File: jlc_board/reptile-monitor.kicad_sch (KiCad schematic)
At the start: 49 parts, among them J1 USB_C_Receptacle_USB2.0, J2 AC_IN, J3 Conn_01x08, J7 LOAD0, J8 LOAD1, K1 1462041-7, K2 1462041-7, SW1 RESET, SW2 BOOT, U1 ESP32-S2-WROVER, U2 TPS2112PW, U3 AP2112K-3.3, U4 MDC3105LT1G, U5 MDC3105LT1G, Y1 32.768KHz 12.5p

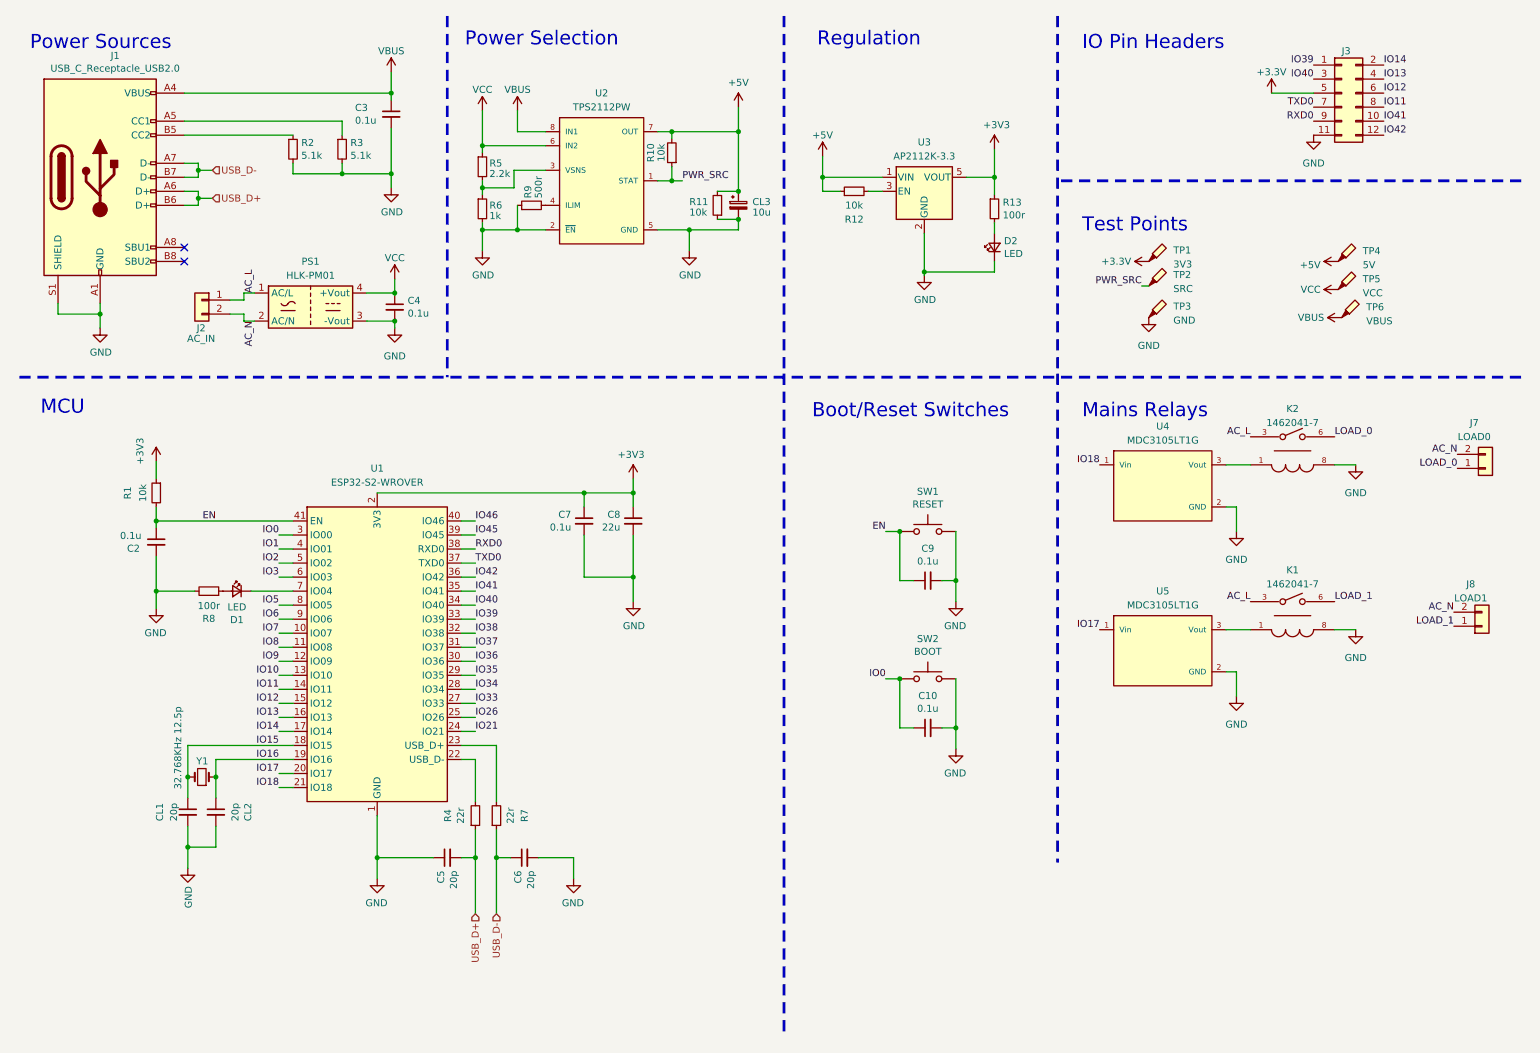
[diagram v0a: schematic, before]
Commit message: Rev2 - Change to Panasonic relays as they're actually attainable and cheaper.
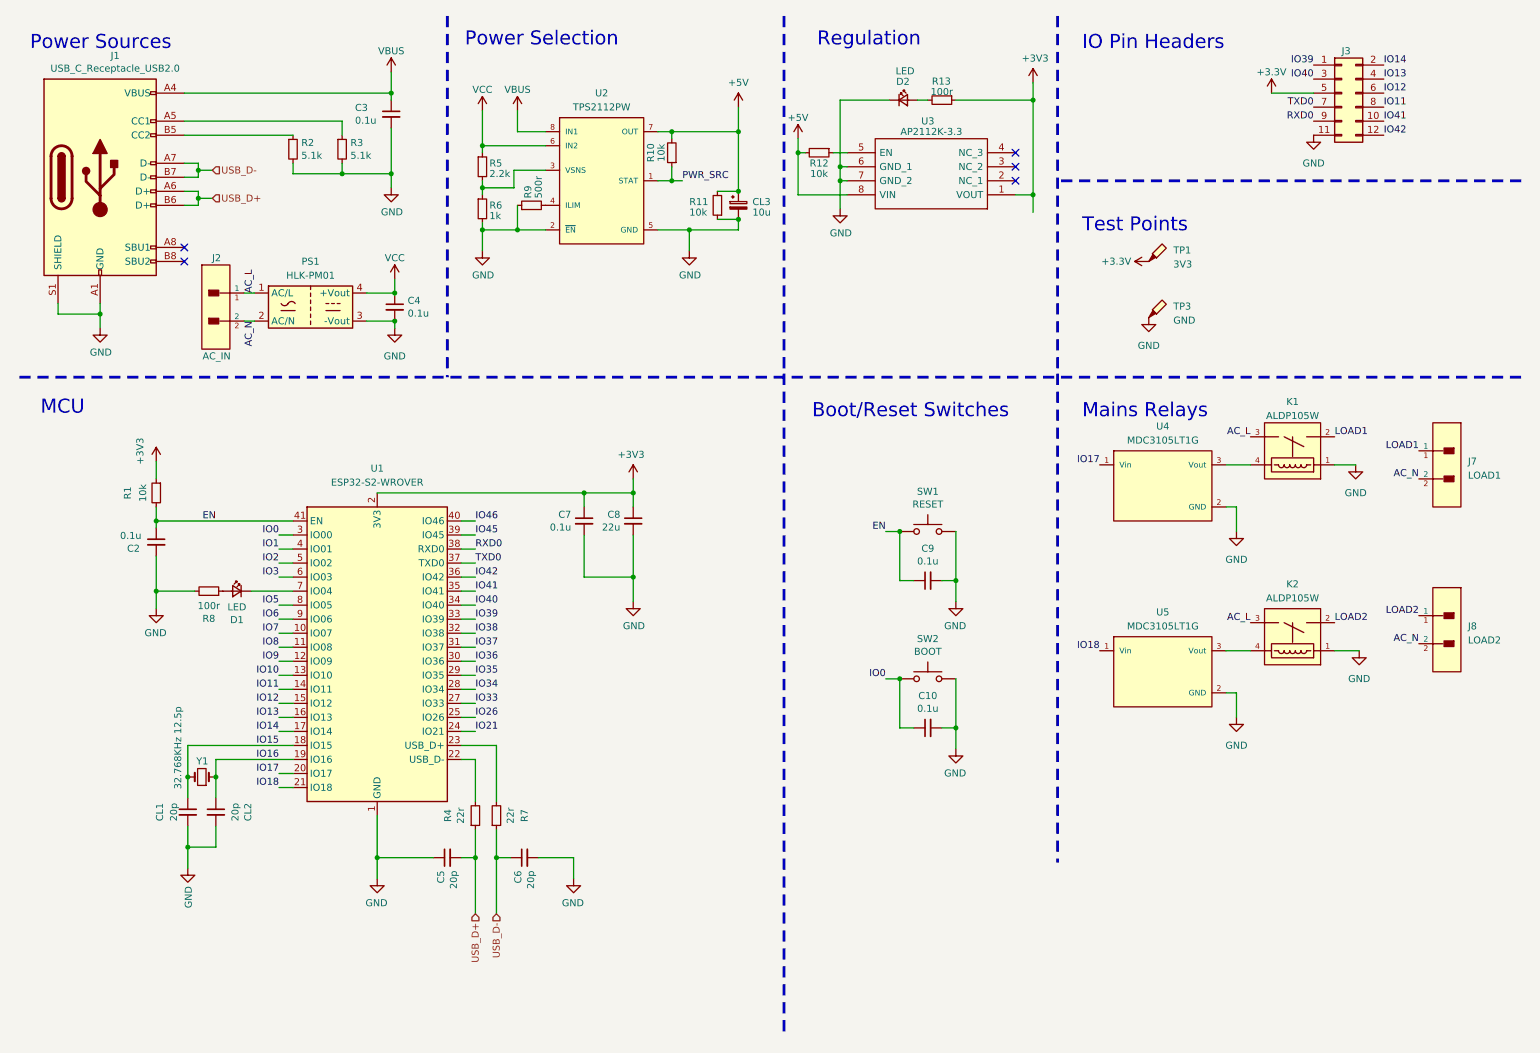
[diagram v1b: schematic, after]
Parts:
- removed K1, K2: 1462041-7, Reptile_Monitor:TE_Connectivity-1462041-7-0-0, symbol Reptile_Monitor:1462041-7
- removed TP2: SRC, TestPoint:TestPoint_THTPad_1.0x1.0mm_Drill0.5mm, symbol Connector:TestPoint_Probe
- removed TP4: 5V, TestPoint:TestPoint_THTPad_1.0x1.0mm_Drill0.5mm, symbol Connector:TestPoint_Probe
- removed TP5: VCC, TestPoint:TestPoint_THTPad_1.0x1.0mm_Drill0.5mm, symbol Connector:TestPoint_Probe
- removed TP6: VBUS, TestPoint:TestPoint_THTPad_1.0x1.0mm_Drill0.5mm, symbol Connector:TestPoint_Probe
- added K1, K2: ALDP105W, reptile-monitor:Panasonic-ALDP105W-Manufacturer_Recommended, symbol Reptile_Monitor:ALDP105W
- J2: footprint Connector_Molex:Molex_Micro-Fit_3.0_43650-0215_1x02_P3.00mm_Vertical -> reptile-monitor:Molex-43650-0215-0-0-MFG; symbol Connector_Generic:Conn_01x02 -> Reptile_Monitor:43650-0215; 3DS Part Number (none) -> 610-00029; category (none) -> Conn; contact material (none) -> Tin,Brass; current rating (none) -> 8.5A; device class L1 (none) -> Connectors; device class L2 (none) -> Board to Board Connectors; device class L3 (none) -> unset; digikey description (none) -> CONN HEADER 2POS 3MM VERT TIN; digikey part number (none) -> WM1917-ND; footprint url (none) -> http://www.molex.com/pdm_docs/sd/436500200_sd.pdf; height (none) -> 10.15mm; is connector (none) -> yes; is male (none) -> yes; lead free (none) -> yes; library id (none) -> bd6a551cc925a413; manufacturer (none) -> Molex; mouser description (none) -> Headers & Wire Housings MICRO-FIT 3.0 HEADER; mouser part number (none) -> 538-43650-0215; number of contacts (none) -> 2; number of rows (none) -> 1; package (none) -> CONN_2POS; rohs (none) -> yes; temperature range high (none) -> +105°C; temperature range low (none) -> -40°C; voltage rating (none) -> 600V
- J7: value LOAD0 -> LOAD1; footprint Connector_Molex:Molex_Micro-Fit_3.0_43650-0215_1x02_P3.00mm_Vertical -> reptile-monitor:Molex-43650-0215-0-0-MFG; symbol Connector_Generic:Conn_01x02 -> Reptile_Monitor:43650-0215; 3DS Part Number (none) -> 610-00029; category (none) -> Conn; contact material (none) -> Tin,Brass; current rating (none) -> 8.5A; device class L1 (none) -> Connectors; device class L2 (none) -> Board to Board Connectors; device class L3 (none) -> unset; digikey description (none) -> CONN HEADER 2POS 3MM VERT TIN; digikey part number (none) -> WM1917-ND; footprint url (none) -> http://www.molex.com/pdm_docs/sd/436500200_sd.pdf; height (none) -> 10.15mm; is connector (none) -> yes; is male (none) -> yes; lead free (none) -> yes; library id (none) -> bd6a551cc925a413; manufacturer (none) -> Molex; mouser description (none) -> Headers & Wire Housings MICRO-FIT 3.0 HEADER; mouser part number (none) -> 538-43650-0215; number of contacts (none) -> 2; number of rows (none) -> 1; package (none) -> CONN_2POS; rohs (none) -> yes; temperature range high (none) -> +105°C; temperature range low (none) -> -40°C; voltage rating (none) -> 600V
- J8: value LOAD1 -> LOAD2; footprint Connector_Molex:Molex_Micro-Fit_3.0_43650-0215_1x02_P3.00mm_Vertical -> reptile-monitor:Molex-43650-0215-0-0-MFG; symbol Connector_Generic:Conn_01x02 -> Reptile_Monitor:43650-0215; 3DS Part Number (none) -> 610-00029; category (none) -> Conn; contact material (none) -> Tin,Brass; current rating (none) -> 8.5A; device class L1 (none) -> Connectors; device class L2 (none) -> Board to Board Connectors; device class L3 (none) -> unset; digikey description (none) -> CONN HEADER 2POS 3MM VERT TIN; digikey part number (none) -> WM1917-ND; footprint url (none) -> http://www.molex.com/pdm_docs/sd/436500200_sd.pdf; height (none) -> 10.15mm; is connector (none) -> yes; is male (none) -> yes; lead free (none) -> yes; library id (none) -> bd6a551cc925a413; manufacturer (none) -> Molex; mouser description (none) -> Headers & Wire Housings MICRO-FIT 3.0 HEADER; mouser part number (none) -> 538-43650-0215; number of contacts (none) -> 2; number of rows (none) -> 1; package (none) -> CONN_2POS; rohs (none) -> yes; temperature range high (none) -> +105°C; temperature range low (none) -> -40°C; voltage rating (none) -> 600V
- U3: footprint Package_TO_SOT_SMD:SOT-23-5 -> SamacSys_Parts:SOIC127P600X170-8N; symbol Regulator_Linear:AP2112K-3.3 -> SamacSys_Parts:AP2112M-3.3TRG1; Height (none) -> 1.7; Manufacturer_Name (none) -> Diodes Inc.; Manufacturer_Part_Number (none) -> AP2112M-3.3TRG1; Mouser Part Number (none) -> 621-AP2112M-3.3TRG1; Mouser Price/Stock (none) -> https://www.mouser.co.uk/ProductDetail/Diodes-Incorporated/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
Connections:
- net +3V3: now also U3.1 (VOUT); no longer U3.5 (VOUT)
- net +5V: now also R12.2, U3.8 (VIN); no longer R12.1, U3.1 (VIN)
- net AC_L: now also K1.3 (COM), K2.3 (COM)
- net GND: now also U3.6 (GND_1), U3.7 (GND_2), K1.1, K2.1; no longer U3.2 (GND)
- net IO17: now also U4.1 (Vin); no longer U5.1 (Vin)
- net IO18: now also U5.1 (Vin); no longer U4.1 (Vin)
- net at U5.3 (Vout): now also K2.4
- net at U3.3 (NC_2): no longer R12.2
- net at U4.3 (Vout): now also K1.4
- net LOAD_0 renamed LOAD1
- net LOAD1: now also K1.2 (NO)
- net LOAD_1 renamed LOAD2
- net LOAD2: now also K2.2 (NO)
- new net: R12.1, U3.5 (EN)
- no-connect marks 2 -> 5
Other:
- moved on the sheet: D2, R12, R13, U5

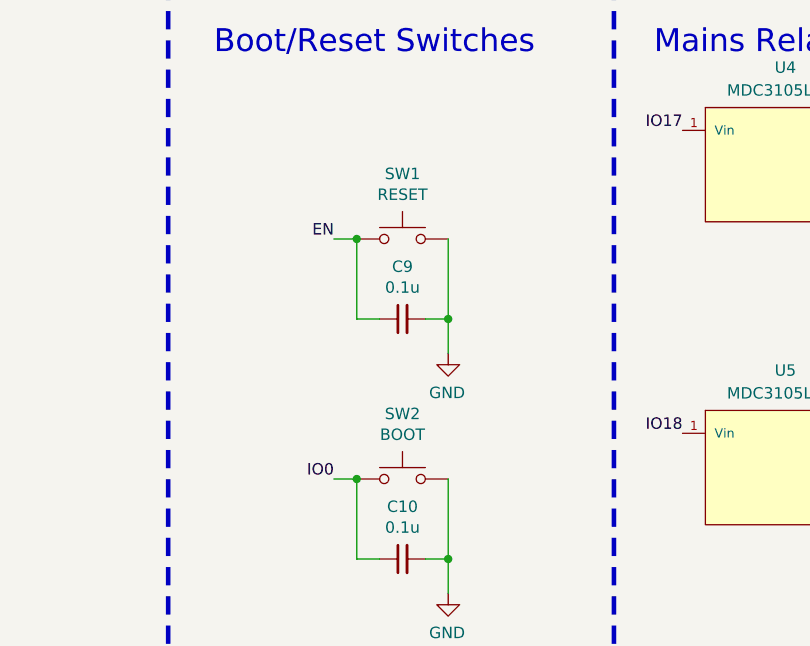
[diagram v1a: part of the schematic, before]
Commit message: Change ALPS to Omron boot and reset buttons cause they're available from Digi-Key
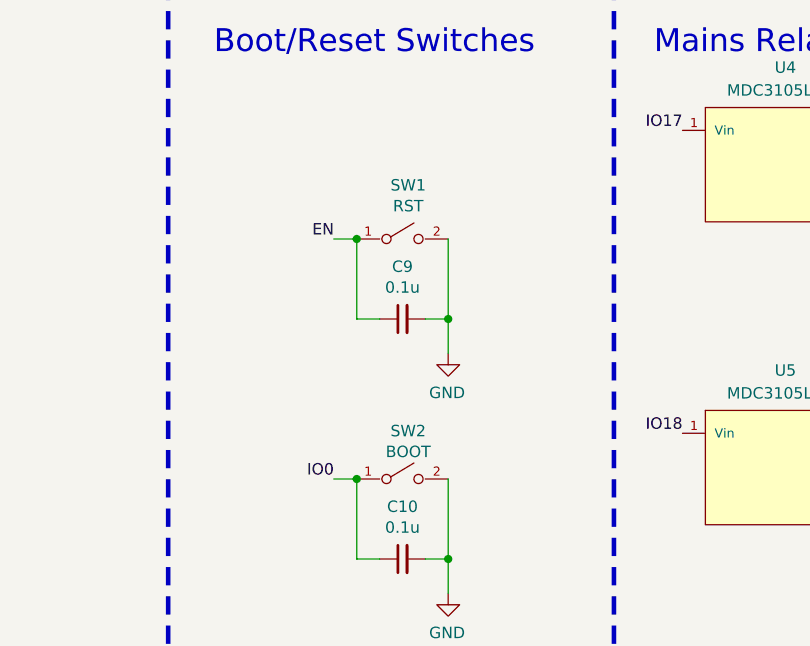
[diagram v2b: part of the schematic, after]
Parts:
- SW1: value RESET -> RST; footprint Reptile_Monitor:Alps_SKRK -> reptile-monitor:Omron-B3U-1000P-MFG; symbol Switch:SW_Push -> Reptile_Monitor:B3U-1000P; ambient temperature range high (none) -> +70°C; ambient temperature range low (none) -> -25°C; automotive (none) -> No; category (none) -> Switch; contact current rating (none) -> 50mA; contact resistance (none) -> 100mΩ; current rating (none) -> 0.05A; device class L1 (none) -> Electromechanical; device class L2 (none) -> Switches; device class L3 (none) -> Tactile Switches; digikey description (none) -> SWITCH TACTILE SPST-NO 0.05A 12V; digikey part number (none) -> SW1020CT-ND; electromechanical life (none) -> 200000Cycles; height (none) -> 1.75mm; lead free (none) -> Yes; library id (none) -> b933800f68cdf4c7; manufacturer (none) -> Omron; mount (none) -> Surface Mount; mouser part number (none) -> 653-B3U-1000P; operating force (none) -> 1.5N; package (none) -> SW_SMT_3MM2_2MM7; rohs (none) -> Yes; temperature range high (none) -> +70°C; temperature range low (none) -> -25°C; throw configuration (none) -> SPST-NO; voltage rating DC (none) -> 12V
- SW2: footprint Reptile_Monitor:Alps_SKRK -> reptile-monitor:Omron-B3U-1000P-MFG; symbol Switch:SW_Push -> Reptile_Monitor:B3U-1000P; ambient temperature range high (none) -> +70°C; ambient temperature range low (none) -> -25°C; automotive (none) -> No; category (none) -> Switch; contact current rating (none) -> 50mA; contact resistance (none) -> 100mΩ; current rating (none) -> 0.05A; device class L1 (none) -> Electromechanical; device class L2 (none) -> Switches; device class L3 (none) -> Tactile Switches; digikey description (none) -> SWITCH TACTILE SPST-NO 0.05A 12V; digikey part number (none) -> SW1020CT-ND; electromechanical life (none) -> 200000Cycles; height (none) -> 1.75mm; lead free (none) -> Yes; library id (none) -> b933800f68cdf4c7; manufacturer (none) -> Omron; mount (none) -> Surface Mount; mouser part number (none) -> 653-B3U-1000P; operating force (none) -> 1.5N; package (none) -> SW_SMT_3MM2_2MM7; rohs (none) -> Yes; temperature range high (none) -> +70°C; temperature range low (none) -> -25°C; throw configuration (none) -> SPST-NO; voltage rating DC (none) -> 12V
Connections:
- net EN: now also SW1.1; no longer SW1.2
- net GND: now also SW1.2, SW2.2; no longer SW1.1, SW2.1
- net IO0: now also SW2.1; no longer SW2.2

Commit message: rev2
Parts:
- removed C3, C4: 0.1u, Capacitor_SMD:C_0603_1608Metric, symbol Device:C_Small
- removed C5, C6: 20p, Capacitor_SMD:C_0603_1608Metric, symbol Device:C_Small
- removed CL3: 10u, Capacitor_SMD:C_0603_1608Metric, symbol Device:C_Polarized_Small
- removed J1: USB_C_Receptacle_USB2.0, Reptile_Monitor:USB_C_Receptacle_HRO_TYPE-C-31-M-12, symbol Connector:USB_C_Receptacle_USB2.0
- removed R10, R11: 10k, Resistor_SMD:R_0603_1608Metric, symbol Device:R_Small
- removed R2, R3: 5.1k, Resistor_SMD:R_0603_1608Metric, symbol Device:R_Small
- removed R4, R7: 22r, Resistor_SMD:R_0603_1608Metric, symbol Device:R_Small
- removed R5: 2.2k, Resistor_SMD:R_0603_1608Metric, symbol Device:R_Small
- removed R6: 1k, Resistor_SMD:R_0603_1608Metric, symbol Device:R_Small
- removed R9: 500r, Resistor_SMD:R_0603_1608Metric, symbol Device:R_Small
- removed TP1: 3V3, TestPoint:TestPoint_THTPad_1.0x1.0mm_Drill0.5mm, symbol Connector:TestPoint_Probe
- removed TP3: GND, TestPoint:TestPoint_THTPad_1.0x1.0mm_Drill0.5mm, symbol Connector:TestPoint_Probe
- removed U1: ESP32-S2-WROVER, RF_Module:ESP32-S2-WROVER, symbol RF_Module:ESP32-S2-WROVER
- removed U2: TPS2112PW, Reptile_Monitor:Texas_Instruments-TPS2112PW, symbol Reptile_Monitor:TPS2112PW
- removed U4, U5: MDC3105LT1G, Reptile_Monitor:ON_Semiconductor-318-08-01_2018-AS, symbol Reptile_Monitor:MDC3105LT1G
- added C1: 1u, Capacitor_SMD:C_0805_2012Metric, symbol Device:C_Small
- added F1: 39208000440, SamacSys_Parts:TO508P400X850X850-2P, symbol SamacSys_Parts:39215000000
- added IC1: ESP32-WROVER-E_M213EH6464PH3Q0_, SamacSys_Parts:ESP32WROVEREM213EH6464PH3Q0, symbol SamacSys_Parts:ESP32-WROVER-E_M213EH6464PH3Q0_
- added J1: UART, Connector_PinHeader_2.54mm:PinHeader_1x04_P2.54mm_Vertical, symbol Connector_Generic:Conn_01x04
- added RV1: Varistor, Varistor:RV_Disc_D7mm_W3.4mm_P5mm, symbol Device:Varistor
- added U1: NUD3105DMT1G, reptile-monitor:ON_Semi-318F-0-0-0, symbol Reptile_Monitor:NUD3105DMT1G
- C2: value 0.1u -> 1u; footprint Capacitor_SMD:C_0603_1608Metric -> Capacitor_SMD:C_0805_2012Metric; LCSC C14663 -> (none); Series (none) -> X7R or X5R
- R1: LCSC C99198 -> (none)
- Y1: footprint Reptile_Monitor:Crystal_SMD_3215-2Pin_3.2x1.5mm -> reptile-monitor:Crystal_SMD_3215-2Pin_3.2x1.5mm
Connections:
- net IO11 is gone; now on net IO36: J3.8 (Pin_8)
- net IO40 is gone; now on net IO15: J3.3 (Pin_3)
- net VCC is gone; now on net +5V: PS1.4 (+Vout)
- net +3V3: now also C2.2, IC1.2 (3V3), J1.1 (Pin_1); no longer J3.5 (Pin_5), R1.1
- net +5V: now also K1.1, K2.1, C1.1
- net AC_L: now also F1.1; no longer K1.3 (COM), K2.3 (COM), PS1.1 (AC/L)
- net AC_N: now also RV1.1
- net EN: now also R1.1, IC1.3 (EN); no longer C2.1, C9.1, R1.2, SW1.1
- net GND: now also C2.1, C1.2, IC1.1 (GND_1), IC1.15 (GND_2), IC1.38 (GND_3), IC1.39 (GND_4), IC1.40 (GND_5), IC1.41 (GND_6), IC1.42 (GND_7), IC1.43 (GND_8), IC1.44 (GND_9), IC1.45 (GND_10), IC1.46 (GND_11), IC1.47 (GND_12), J1.4 (Pin_4), U1.1 (1_Source), U1.4 (2_Source); no longer C2.2, J3.11 (Pin_11), K1.1, K2.1
- net IO0: now also IC1.25 (IO0)
- net IO12: now also IC1.14 (IO12), U1.5 (2_Gate); no longer J3.6 (Pin_6)
- net IO13: now also D1.1 (K), IC1.16 (IO13); no longer J3.4 (Pin_4)
- net IO14: now also IC1.13 (IO14), U1.2 (1_Gate); no longer J3.2 (Pin_2)
- net IO15: now also IC1.23 (IO15); no longer CL1.1, Y1.2
- net IO18: now also J3.1 (Pin_1), IC1.30 (IO18)
- net IO2: now also IC1.24 (IO2)
- net IO21: now also J3.5 (Pin_5), IC1.33 (IO21)
- net IO26: now also J3.11 (Pin_11), IC1.11 (IO26)
- net IO36: now also IC1.4 (SENSOR_VP)
- net IO39: now also J3.9 (Pin_9), IC1.5 (SENSOR_VN); no longer J3.1 (Pin_1)
- net IO5: now also J3.4 (Pin_4), IC1.29 (IO5)
- net RXD0: now also IC1.34 (RXD0), J1.2 (Pin_2); no longer J3.9 (Pin_9)
- net TXD0: now also IC1.35 (TXD0), J1.3 (Pin_3); no longer J3.7 (Pin_7)
- net PWR_EN: now reaches R12.1, U3.5 (EN)
- net RLY1: now reaches K1.4
- net RLY1: now also U1.6 (1_Drain)
- net RLY2: now reaches K2.4
- net RLY2: now also U1.3 (2_Drain)
- net IO16: no longer names the net of CL2.1, Y1.1
- net IO16: now also IC1.9 (IO33)
- net IO41 renamed IO25
- net IO25: now also IC1.10 (IO25)
- net IO42 renamed IO27
- net IO27: now also IC1.12 (IO27)
- new net: C9.1, R1.2, SW1.1
- new net: CL1.1, IC1.8 (IO32), Y1.2
- new net FUSED_AC_L: F1.2, K1.3 (COM), K2.3 (COM), PS1.1 (AC/L), RV1.2
- new net IO19: IC1.31 (IO19), J3.2 (Pin_2)
- new net IO22: IC1.36 (IO22), J3.6 (Pin_6)
- new net IO23: IC1.37 (IO23), J3.7 (Pin_7)
- no-connect marks 5 -> 10
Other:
- note added: "Power Source"
- note removed: "Power Selection"
- note removed: "Power Sources"
- note removed: "Test Points"
- moved on the sheet: C10, C7, C8, C9, D1, D2, J2, J3, J7, J8, PS1, R12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
